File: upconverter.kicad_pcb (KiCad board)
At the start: 2 copper layers, 35 parts, among them J1 Barrel_Jack, J2 SMA_F, J3 SMA_F, U1 L7805, U2 TPS71533__SC70, U3 SA602A, X1 XO32

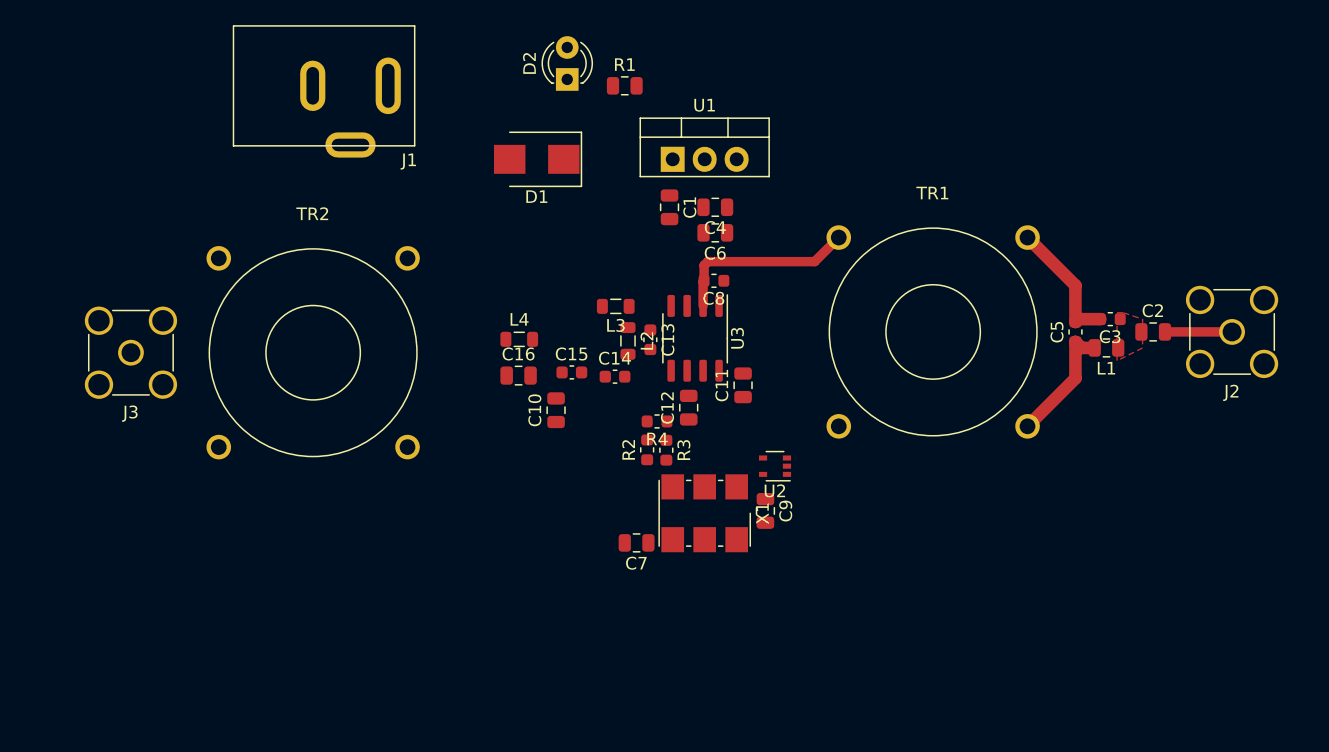
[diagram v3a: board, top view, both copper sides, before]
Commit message: Board edge, tracks. Need to finish DRC fixes & JLCPCB setup
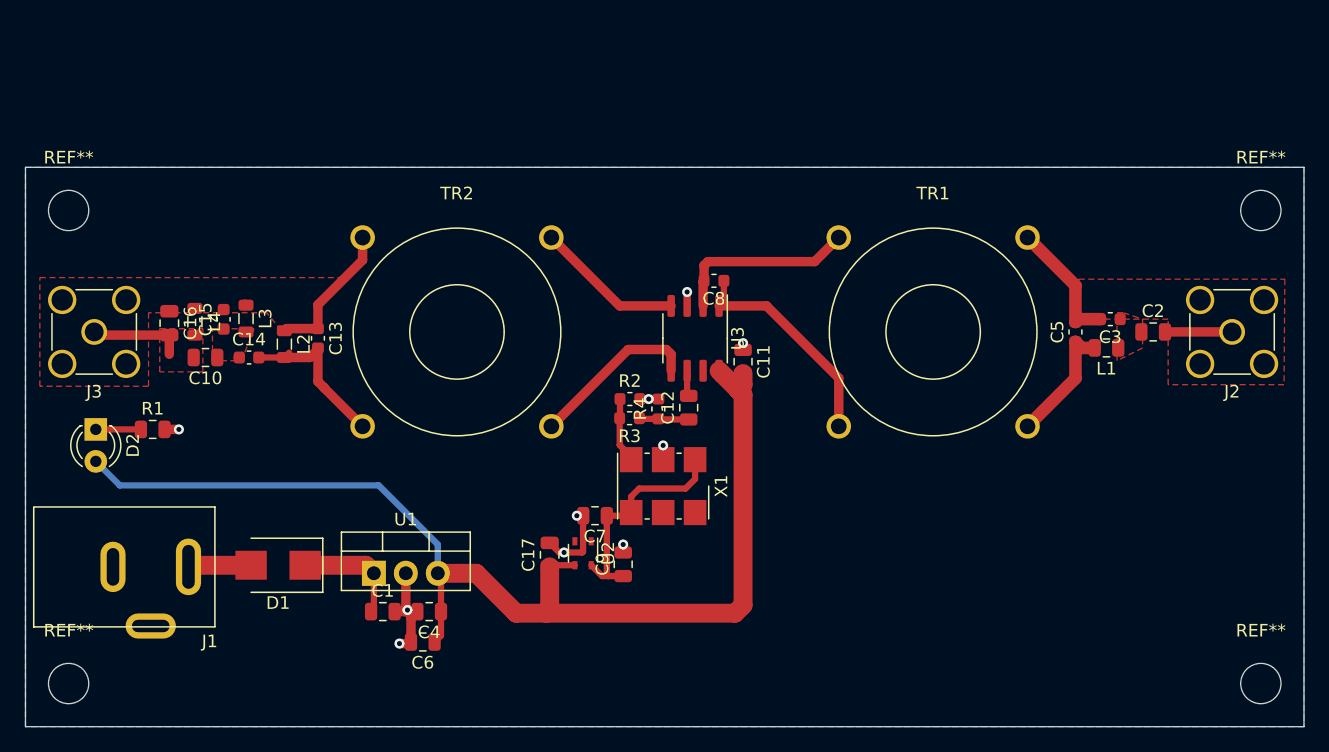
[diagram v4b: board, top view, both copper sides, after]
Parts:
- added C17: C_0805_2012Metric, Capacitor_SMD:C_0805_2012Metric, F.Cu at (83.2, 93.9)
- added REF**: MountingHole_3.2mm_M3, MountingHole:MountingHole_3.2mm_M3, F.Cu at (139.7, 104.1)
- added REF**: MountingHole_3.2mm_M3, MountingHole:MountingHole_3.2mm_M3, F.Cu at (45.0, 104.1)
- added REF**: MountingHole_3.2mm_M3, MountingHole:MountingHole_3.2mm_M3, F.Cu at (139.7, 66.5)
- added REF**: MountingHole_3.2mm_M3, MountingHole:MountingHole_3.2mm_M3, F.Cu at (45.0, 66.5)
- moved D2 46.7 mm to (47.1, 83.9), turned to 270 degrees
- moved R1 46.4 mm to (51.6, 83.9)
- moved J1 41.4 mm to (54.5, 94.9)
- moved U1 40.6 mm to (69.2, 95.4)
- moved C6 40.0 mm to (73.1, 100.8)
- moved C1 39.4 mm to (69.9, 98.4), turned to 0 degrees
- moved C4 39.4 mm to (73.6, 98.4)
- moved D1 38.3 mm to (61.6, 94.7)
- moved L3 29.4 mm to (59.1, 75.1), turned to 270 degrees
- moved C14 29.1 mm to (59.3, 78.2)
- moved C10 28.2 mm to (55.8, 78.2), turned to 180 degrees
- moved C16 28.1 mm to (53.0, 75.5), turned to 270 degrees
- moved C15 28.0 mm to (57.3, 75.2), turned to 90 degrees
- moved L2 27.3 mm to (62.1, 77.2)
- moved C13 26.4 mm to (64.8, 76.7)
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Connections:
- J3 pad 1: Net-(J3-Pad1) -> Net-(C10-Pad2)
- J3 pad 2: Net-(J3-Pad2) -> Net-(C13-Pad1)
- TR2 pad 1: Net-(C10-Pad2) -> Net-(TR2-Pad1)
- U3 pad 4: Net-(C13-Pad1) -> Net-(TR2-Pad2)
- U3 pad 5: Net-(C13-Pad2) -> Net-(TR2-Pad1)
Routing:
- net +5V: track 0.00 -> 90.5 mm
- net GND: track 0.00 -> 20.9 mm, vias 0 -> 10
- net +3V3: track 0.00 -> 18.2 mm
- net Net-(C8-Pad1): track 0.00 -> 17.9 mm
- net Net-(TR2-Pad1): track 0.00 -> 13.5 mm
- net Net-(C13-Pad2): track 0.00 -> 13.3 mm
- net Net-(C13-Pad1): track 0.00 -> 11.9 mm
- net Net-(TR2-Pad2): track 0.00 -> 11.8 mm
- net Net-(C1-Pad1): track 0.00 -> 8.86 mm
- net Net-(C10-Pad2): track 0.00 -> 7.74 mm
- net Net-(R2-Pad1): track 0.00 -> 5.21 mm
- net Net-(D1-Pad2): track 0.00 -> 5.02 mm
- net Net-(C12-Pad1): track 0.00 -> 3.95 mm
- net Net-(D2-Pad1): track 0.00 -> 3.59 mm
- net Net-(C12-Pad2): track 0.00 -> 2.05 mm
- added copper zone on B.Cu, net GND
- added copper zone on F.Cu, net Net-(C10-Pad1)
- added copper zone on F.Cu, net Net-(C10-Pad2)
- added copper zone on F.Cu, net Net-(C13-Pad1)
- added copper zone on F.Cu, net Net-(C3-Pad2)
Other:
- board outline added: 101.6 x 44.5 mm

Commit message: gerbers
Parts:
- moved C7 0.35 mm to (86.4, 90.8)
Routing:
- net Net-(C3-Pad2): track 10.4 -> 20.4 mm
- net Net-(C13-Pad1): track 11.9 -> 14.0 mm
- net Net-(C10-Pad1): track 0.23 -> 2.10 mm
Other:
- board text added: "JLCJLCJLCJLC"
- board text added: "Upconverter rev 0 Zach Martin"

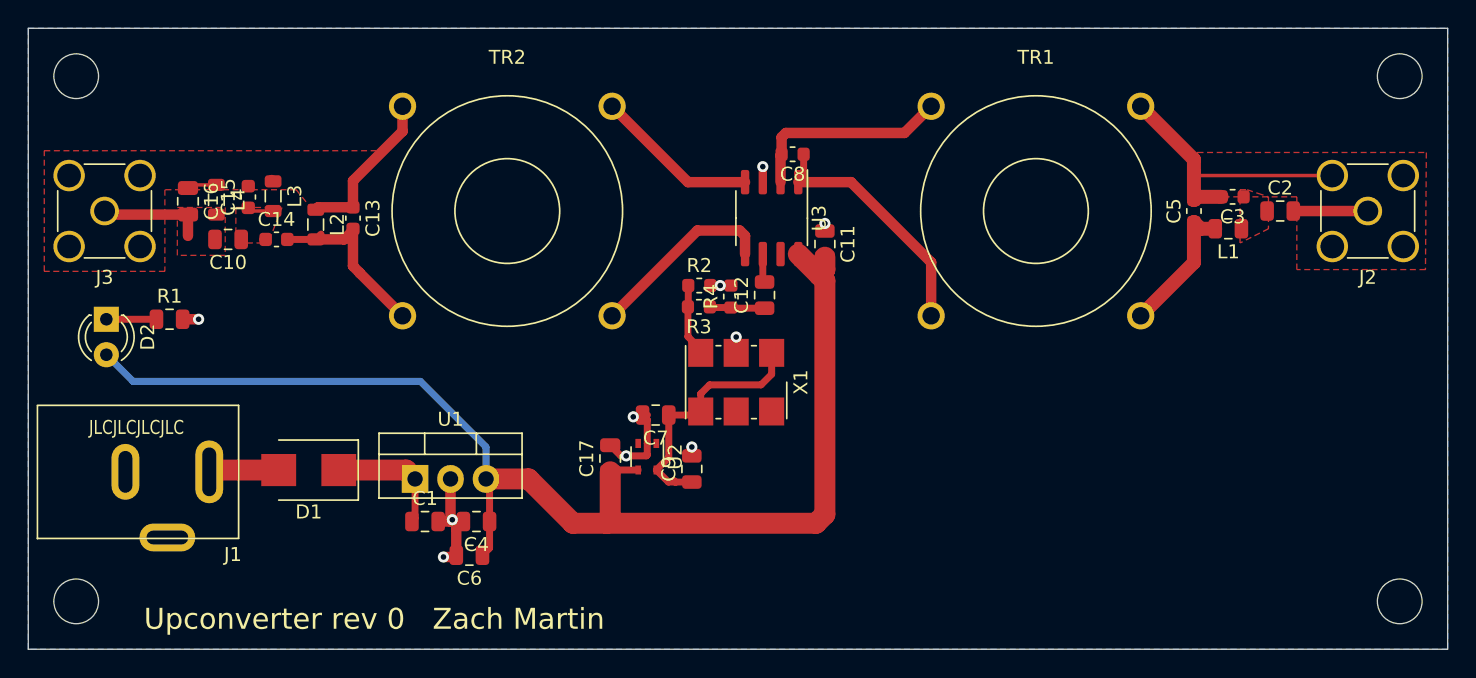
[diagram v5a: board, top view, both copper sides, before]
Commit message: Layout for single ended vers. TODO:needs silk screen text, fix ref des, lay tracks/fills, board size, TESTTT
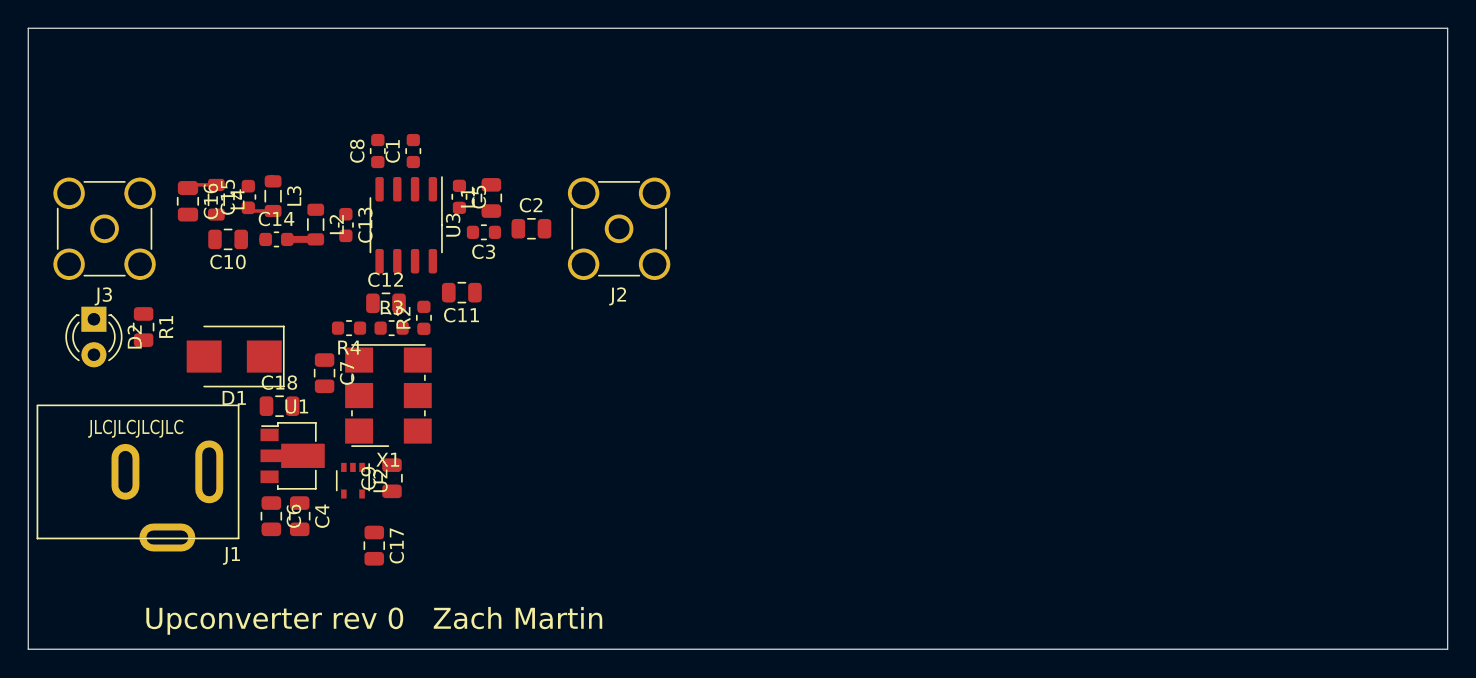
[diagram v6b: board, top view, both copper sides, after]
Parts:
- removed REF** (x4): MountingHole_3.2mm_M3, MountingHole:MountingHole_3.2mm_M3
- removed TR1, TR2: TRANSF1, ZAM_Custom:fair-rite_2643625002
- added C18: 10uF, Capacitor_SMD:C_0805_2012Metric, F.Cu at (59.5, 90.2)
- C1: value 10uF -> 10nF; footprint Capacitor_SMD:C_0805_2012Metric -> Capacitor_SMD:C_0603_1608Metric
- C17: value C_0805_2012Metric -> 100nF
- C4: value 10nF -> 10uF
- C8: value 100pF -> 10nF
- U1: value L7805 -> LM2936-5.0; footprint Package_TO_SOT_THT:TO-220-3_Vertical -> Package_TO_SOT_SMD:SOT-89-3
- moved C3 53.7 mm to (74.1, 77.7)
- moved C2 53.6 mm to (77.5, 77.5)
- moved J2 53.6 mm to (83.8, 77.5)
- moved L1 52.8 mm to (74.7, 75.3), turned to 90 degrees
- moved C5 52.6 mm to (72.4, 75.2), turned to 270 degrees
- moved C8 29.7 mm to (66.5, 71.9), turned to 90 degrees
- moved R4 27.4 mm to (64.5, 84.6), turned to 180 degrees
- moved C12 27.1 mm to (67.1, 82.8), turned to 0 degrees
- moved C1 26.5 mm to (69.1, 71.9), turned to 90 degrees
- moved C11 26.2 mm to (72.6, 82.0), turned to 180 degrees
- moved U3 26.2 mm to (68.6, 77.2)
- moved X1 24.9 mm to (67.3, 89.4), turned to 180 degrees
- moved C7 23.9 mm to (62.7, 87.8), turned to 270 degrees
- moved R3 22.0 mm to (67.5, 84.6), turned to 0 degrees
- moved C9 21.5 mm to (67.6, 95.3)
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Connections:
- C13 pad 1: Net-(C13-Pad1) -> GND
- C15 pad 2: Net-(C13-Pad1) -> GND
- C16 pad 1: Net-(C13-Pad1) -> GND
- C3 pad 2: Net-(C3-Pad2) -> GND
- C5 pad 2: Net-(C3-Pad2) -> GND
- C8 pad 2: Net-(C8-Pad2) -> GND
- D1 pad 1: Net-(C1-Pad1) -> Net-(C18-Pad1)
- J2 pad 2: Net-(C3-Pad2) -> GND
- J3 pad 2: Net-(C13-Pad1) -> GND
- L2 pad 1: Net-(C13-Pad1) -> GND
- L3 pad 1: Net-(C13-Pad1) -> GND
- L4 pad 1: Net-(C13-Pad1) -> GND
- U1 pad 1: Net-(C1-Pad1) -> Net-(C18-Pad1)
- U3 pad 1: Net-(C8-Pad1) -> Net-(C5-Pad1)
- U3 pad 2: Net-(C8-Pad2) -> Net-(C1-Pad1)
- U3 pad 4: Net-(TR2-Pad2) -> Net-(C8-Pad1)
- U3 pad 5: Net-(TR2-Pad1) -> Net-(C13-Pad2)
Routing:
- net +5V: track 90.5 -> 0.00 mm
- net Net-(C3-Pad2): track 20.4 -> 0.00 mm
- net +3V3: track 18.2 -> 0.00 mm
- net GND: track 20.6 -> 2.57 mm, vias 10 -> 0
- net Net-(C8-Pad1): track 17.9 -> 0.00 mm
- net Net-(C8-Pad2): track 14.9 -> 0.00 mm
- net Net-(C13-Pad1): track 14.0 -> 0.00 mm
- net Net-(TR2-Pad1): track 13.5 -> 0.00 mm
- net Net-(TR2-Pad2): track 11.8 -> 0.00 mm
- net Net-(C13-Pad2): track 13.3 -> 2.03 mm
- net Net-(C5-Pad1): track 10.0 -> 0.00 mm
- net Net-(C1-Pad1): track 8.86 -> 0.00 mm
- net Net-(C10-Pad2): track 7.74 -> 0.14 mm
- net Net-(C2-Pad2): track 5.33 -> 0.00 mm
- net Net-(R2-Pad1): track 5.21 -> 0.00 mm
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- removed copper zone on B.Cu, net GND
- removed copper zone on F.Cu, net Net-(C10-Pad1)
- removed copper zone on F.Cu, net Net-(C10-Pad2)
- removed copper zone on F.Cu, net Net-(C13-Pad1)
- removed copper zone on F.Cu, net Net-(C2-Pad1)
- removed copper zone on F.Cu, net Net-(C3-Pad2)
